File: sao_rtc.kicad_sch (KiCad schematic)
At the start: 8 parts, among them J1 Conn_02x03_Odd_Even, U1 PCF8563DRG, Y1 Crystal

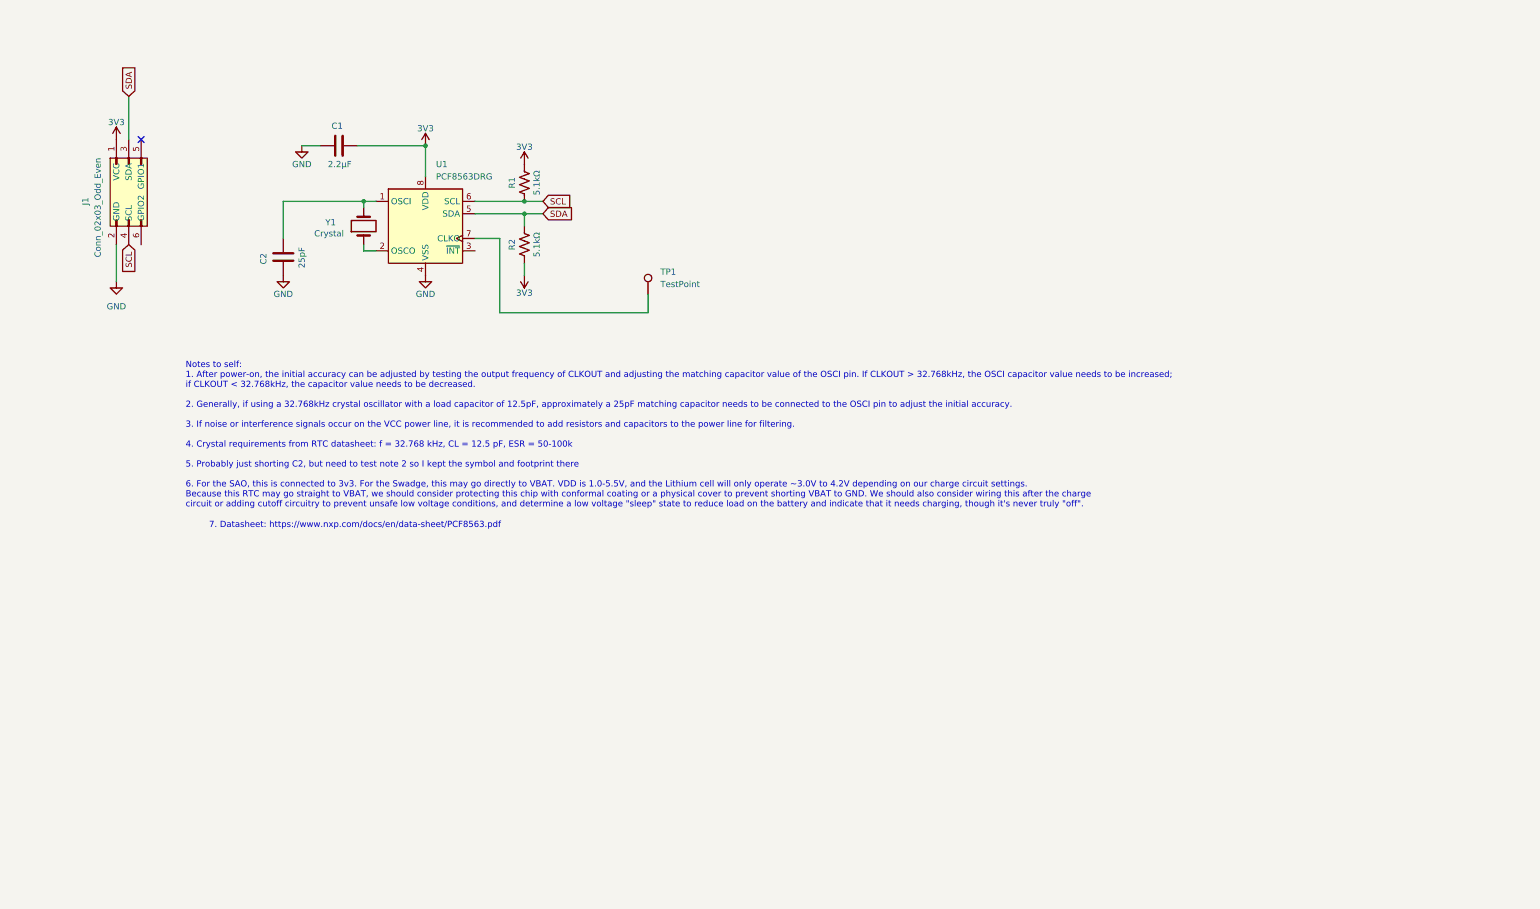
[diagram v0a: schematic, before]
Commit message: scope creep is a hell of a drug
Add AW320001 BMS and associated stuff
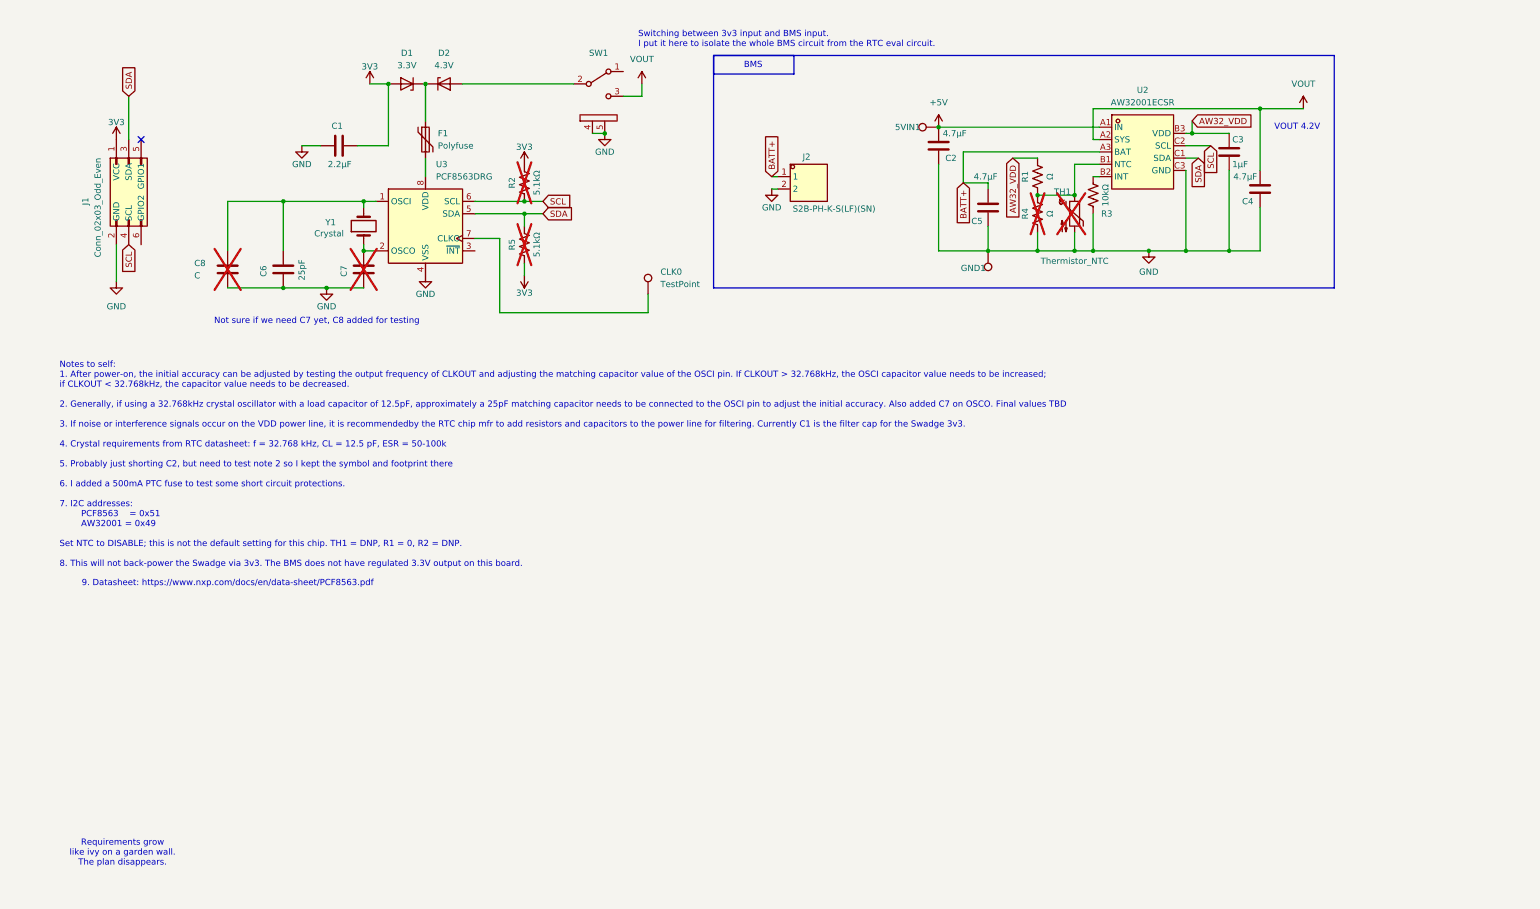
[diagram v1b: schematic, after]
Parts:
- added 5VIN1, GND1: TestPoint, TestPoint:TestPoint_Loop_D2.50mm_Drill1.0mm, symbol Connector:TestPoint
- added C2, C4, C5: 4.7μF, sao:C_0603_1608Metric, symbol Swadge_Parts:C
- added C3: 1μF, sao:C_0603_1608Metric, symbol Swadge_Parts:C
- added C7: (no value), C_0603_1608Metric, symbol Swadge_Parts:C
- added C8: C, Capacitor_THT:C_Disc_D3.0mm_W1.6mm_P2.50mm, symbol Device:C
- added D1: 3.3V, Diode_SMD:D_SOD-323_HandSoldering, symbol Device:D_Zener
- added D2: 4.3V, Diode_SMD:D_SOD-323_HandSoldering, symbol Device:D_Zener
- added F1: Polyfuse, Fuse:Fuse_0805_2012Metric, symbol Device:Polyfuse
- added J2: S2B-PH-K-S(LF)(SN), Connector_PinHeader_2.00mm:PinHeader_1x02_P2.00mm_Horizontal, symbol Swadge_Parts:S2B-PH-K-S(LF)(SN)
- added R1, R4: Ω, Resistor_SMD:R_0603_1608Metric, symbol Swadge_Parts:R_US
- added R3: 10kΩ, Resistor_SMD:R_0603_1608Metric, symbol Swadge_Parts:R_US
- added SW1: SW_SPDT_1825232-1, Swadge_Parts:1825232-1, symbol Swadge_Parts:SW_SPDT_1825232-1
- added TH1: Thermistor_NTC, Resistor_SMD:R_0603_1608Metric, symbol Swadge_Parts:Thermistor_NTC
- added U2: AW32001ECSR, Package_CSP:WLCSP-9_1.21x1.22mm_Layout3x3_P0.4mm, symbol Swadge_Parts:AW32001ECSR
- R2: renamed from R1; now not fitted; now left out of the parts list
- R5: renamed from R2; now not fitted; now left out of the parts list
- renumbered C2 to C6, TP1 to CLK0, U1 to U3
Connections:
- net 3V3: now also D1.2 (A); no longer U3.8 (VDD)
- net GND: now also C2.2, C3.2, C4.2, C5.2, C7.2, C8.2, GND1.1, J2.2, R3.1, R4.1, SW1.4 (D), SW1.5 (E), TH1.2, U2.C3 (GND)
- net SCL: now also U2.C2 (SCL)
- net SDA: now also U2.C1 (SDA)
- net at C6.1, U3.1 (OSCI), Y1.2: now also C8.1
- net at U3.2 (OSCO), Y1.1: now also C7.1
- new net: R1.1, R4.2, TH1.1, U2.B1 (NTC)
- new net: R3.2, U2.B2 (INT)
- new net: D1.1 (K), D2.1 (K), F1.1
- new net: F1.2, U3.8 (VDD)
- new net: D2.2 (A), SW1.2 (B)
- new net +5V: 5VIN1.1, C2.1, U2.A1 (IN)
- new net AW32_VDD: C3.1, R1.2, U2.B3 (VDD)
- new net BATT+: C5.1, J2.1, U2.A3 (BAT)
- new net VOUT: C4.1, SW1.3 (C), U2.A2 (SYS)
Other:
- note added: "9. Datasheet: https://www.nxp.com/docs/en/data-sheet/PCF8563.pdf"
- note added: "BMS"
- note added: "Not sure if we need C7 yet, C8 added for testing"
- note added: "Requirements grow like ivy on a garden wall. The plan disappears."
- note added: "Switching between 3v3 input and BMS input. I put it here to isolate the whole BMS circuit from the RTC eval circuit."
- note added: "VOUT 4.2V"
- note removed: "7. Datasheet: https://www.nxp.com/docs/en/data-sheet/PCF8563.pdf"
- title: (none) -> SAO for RTC evaluation
- moved on the sheet: C6

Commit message: update schematic for voltage regulation
she creeped my scope until I swadged her
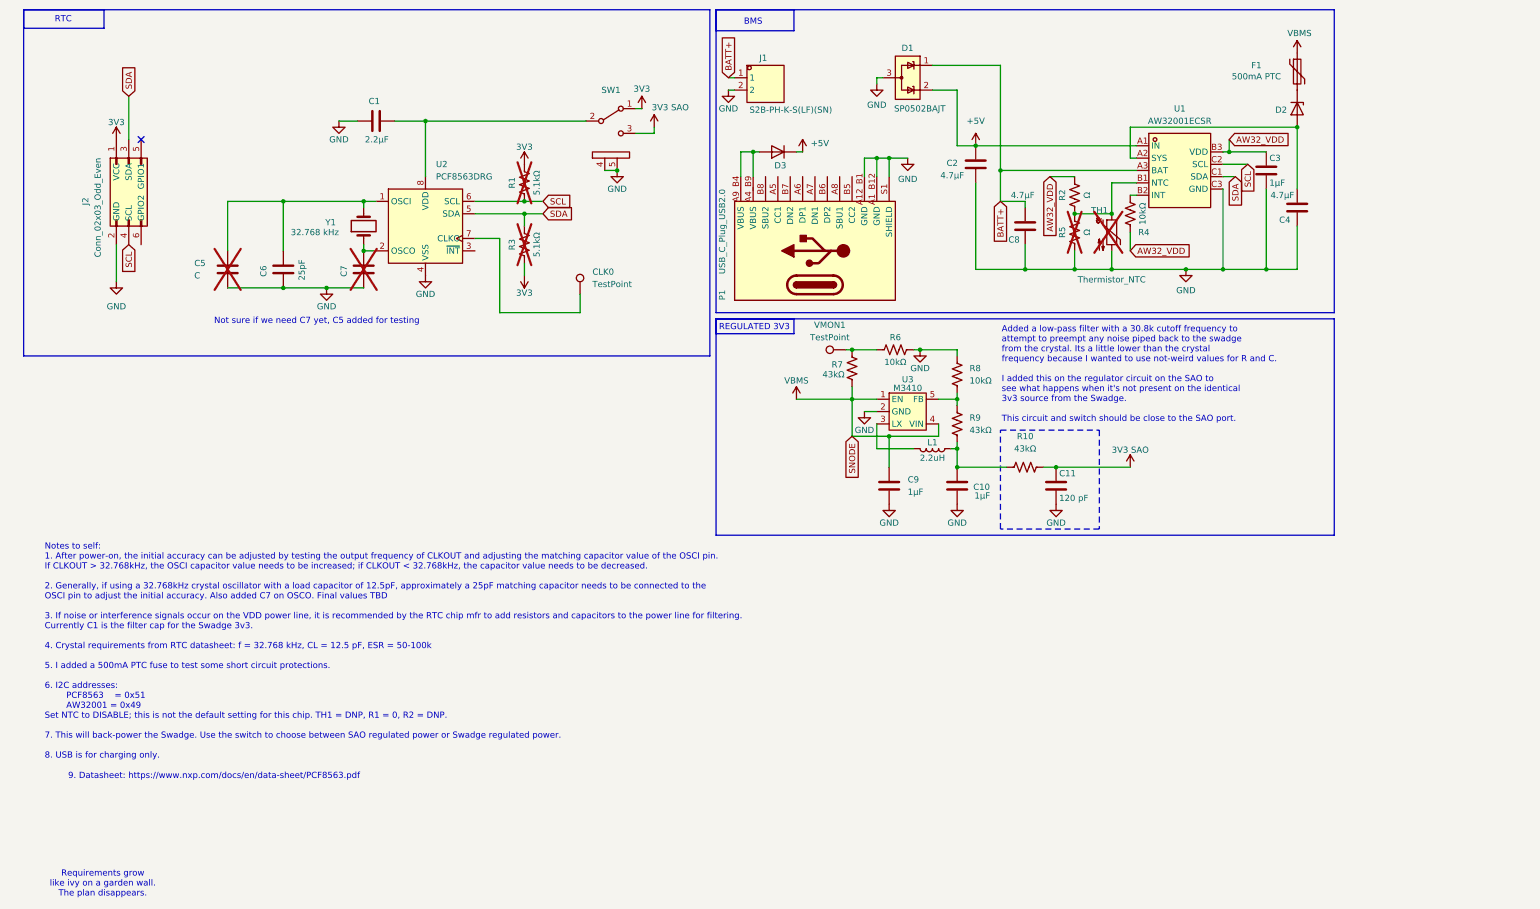
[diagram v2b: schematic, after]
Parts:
- removed 5VIN1, GND1: TestPoint, TestPoint:TestPoint_Loop_D2.50mm_Drill1.0mm, symbol Connector:TestPoint
- removed D1: 3.3V, Diode_SMD:D_SOD-323_HandSoldering, symbol Device:D_Zener
- added C10, C9: 1μF, Capacitor_SMD:C_0603_1608Metric, symbol Swadge_Parts:C
- added C11: 120 pF, Capacitor_SMD:C_0603_1608Metric, symbol Swadge_Parts:C
- added D1: SP0502BAJT, Package_TO_SOT_SMD:SOT-23, symbol Power_Protection:SP0502BAHT
- added D3: D, Diode_SMD:D_SMA, symbol Swadge_Parts:D
- added L1: 2.2uH, Inductor_SMD:L_1008_2520Metric, symbol Swadge_Parts:L
- added P1: USB_C_Plug_USB2.0, Swadge_Parts:USB_C_Receptacle_HRO_TYPE-C-31-M-12, symbol Swadge_Parts:USB_C_Plug_USB2.0
- added R10, R7, R9: 43kΩ, Resistor_SMD:R_0603_1608Metric, symbol Swadge_Parts:R_US
- added R6, R8: 10kΩ, Resistor_SMD:R_0603_1608Metric, symbol Swadge_Parts:R_US
- added U3: M3410, Package_TO_SOT_SMD:SOT-23-5, symbol Swadge_Parts:M3410
- added VMON1: TestPoint, TestPoint:TestPoint_Loop_D2.50mm_Drill1.0mm, symbol Connector:TestPoint
- F1: value Polyfuse -> 500mA PTC
- Y1: value Crystal -> 32.768 kHz
- renumbered C8 to C5, C5 to C8, J2 to J1, J1 to J2, R2 to R1, R1 to R2, R5 to R3, R3 to R4, R4 to R5, U2 to U1, U3 to U2
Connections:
- net +5V: now also D1.2 (K), D3.1 (K)
- net 3V3: now also SW1.1 (A); no longer C1.1
- net AW32_VDD: now also R4.1
- net BATT+: now also D1.1 (K)
- net GND: now also C10.2, C11.2, C9.2, D1.3 (A), P1.A12_B1 (GND), P1.A1_B12 (GND), P1.S1 (SHIELD), R6.2, R8.1, U3.2 (GND); no longer R4.1
- net at D2.1 (K): now also F1.2; no longer F1.1
- net at U2.8 (VDD): now also C1.1, SW1.2 (B); no longer F1.2
- net at D2.2 (A): now also C4.1, U1.A2 (SYS); no longer SW1.2 (B)
- removed net VOUT: C4.1, SW1.3 (C), U1.A2 (SYS)
- new net: R6.1, R7.1, VMON1.1
- new net: L1.2, U3.3 (LX)
- new net: R8.2, R9.1, U3.5 (FB)
- new net: D3.2 (A), P1.A4_B9 (VBUS), P1.A9_B4 (VBUS)
- new net: C10.1, L1.1, R10.1, R9.2
- new net 3V3 SAO: C11.1, R10.2, SW1.3 (C)
- new net VBMS: C9.1, F1.1, R7.2, U3.1 (EN), U3.4 (VIN)
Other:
- note added: "Added a low-pass filter with a 30.8k cutoff frequency to attempt to preempt any noise piped back to the swadge from the crystal. Its a little lower than the crystal frequency because I wanted to use not-weird values for R and C. I added this on the regulator circuit on the SAO to see what happens when it's not present on the identical 3v3 source from the Swadge. This circuit and switch should be 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"
- note added: "Not sure if we need C7 yet, C5 added for testing"
- note added: "REGULATED 3V3"
- note added: "RTC"
- note removed: "Not sure if we need C7 yet, C8 added for testing"
- note removed: "Switching between 3v3 input and BMS input. I put it here to isolate the whole BMS circuit from the RTC eval circuit."
- note removed: "VOUT 4.2V"
- moved on the sheet: C1, C2, C3, C4, C8, CLK0, J1, R2, R4, R5, SW1, TH1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

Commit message: routed and ordered
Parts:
- added D4: 3V3 ON, LED_SMD:LED_0603_1608Metric, symbol Swadge_Parts:LED
- added D5: RTC ON, LED_SMD:LED_0603_1608Metric, symbol Swadge_Parts:LED
- added J3: Conn_02x03_Odd_Even, Connector_PinHeader_2.54mm:PinHeader_2x03_P2.54mm_Vertical, symbol sao:Conn_02x03_Odd_Even
- added R11, R12: 22Ω, Resistor_SMD:R_0603_1608Metric, symbol Swadge_Parts:R_US
- D1: footprint Package_TO_SOT_SMD:SOT-23 -> Package_TO_SOT_SMD:SOT-323_SC-70
- P1: footprint Swadge_Parts:USB_C_Receptacle_HRO_TYPE-C-31-M-12 -> Connector_USB:USB_C_Receptacle_HRO_TYPE-C-31-M-12
- SW1: value SW_SPDT_1825232-1 -> DPDT; footprint Swadge_Parts:1825232-1 -> Button_Switch_SMD:SW_DPDT_CK_JS202011JCQN; symbol Swadge_Parts:SW_SPDT_1825232-1 -> Switch:SW_Slide_DPDT
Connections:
- net 3V3: now also SW1.5 (B), J3.1 (VCC)
- net 3V3 SAO: now also SW1.6 (A), D4.2 (A)
- net GND: now also P1.A1 (GND), P1.A12 (GND), P1.SH (SHIELD), J3.2 (GND), R11.1, R12.1; no longer P1.A12_B1 (GND), P1.A1_B12 (GND), P1.S1 (SHIELD), SW1.4 (D), SW1.5 (E)
- net SCL: now also J3.4 (SCL)
- net SDA: now also J3.3 (SDA)
- net VDD: now reaches C1.1, SW1.2 (B), U2.8 (VDD)
- net VDD: now also D5.2 (A)
- net at J2.5 (GPIO1): now also J3.5 (GPIO1)
- net at J2.6 (GPIO2): now also J3.6 (GPIO2)
- new net: D3.2 (A), P1.A4 (VBUS), P1.A9 (VBUS)
- new net: D5.1 (K), R12.2
- new net: D4.1 (K), R11.2
- no-connect marks 1 -> 0
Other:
- note added: "RTC Power"
- note added: "Swadge Power"
- moved on the sheet: C1, J2, P1
